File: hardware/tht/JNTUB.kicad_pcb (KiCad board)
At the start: 2 copper layers, 41.1 x 110.7 mm, 84 parts, among them J1 PARAM1_CV, J10 B2_HDR_LEFT, J11 B2_HDR_RIGHT, J12 ISP, J2 PARAM2_CV, J3 CLK/TRG, J4 DITTO, J5 OUT1, J6 OUT2, J7 B1_HDR_LEFT, J8 B1_HDR_RIGHT, J9 POWER, Q1 2N3904, Q2 2N3904, Q3 2N3904, U1 ATtiny85, U2 TL074, U3 78L05, U4 79L05

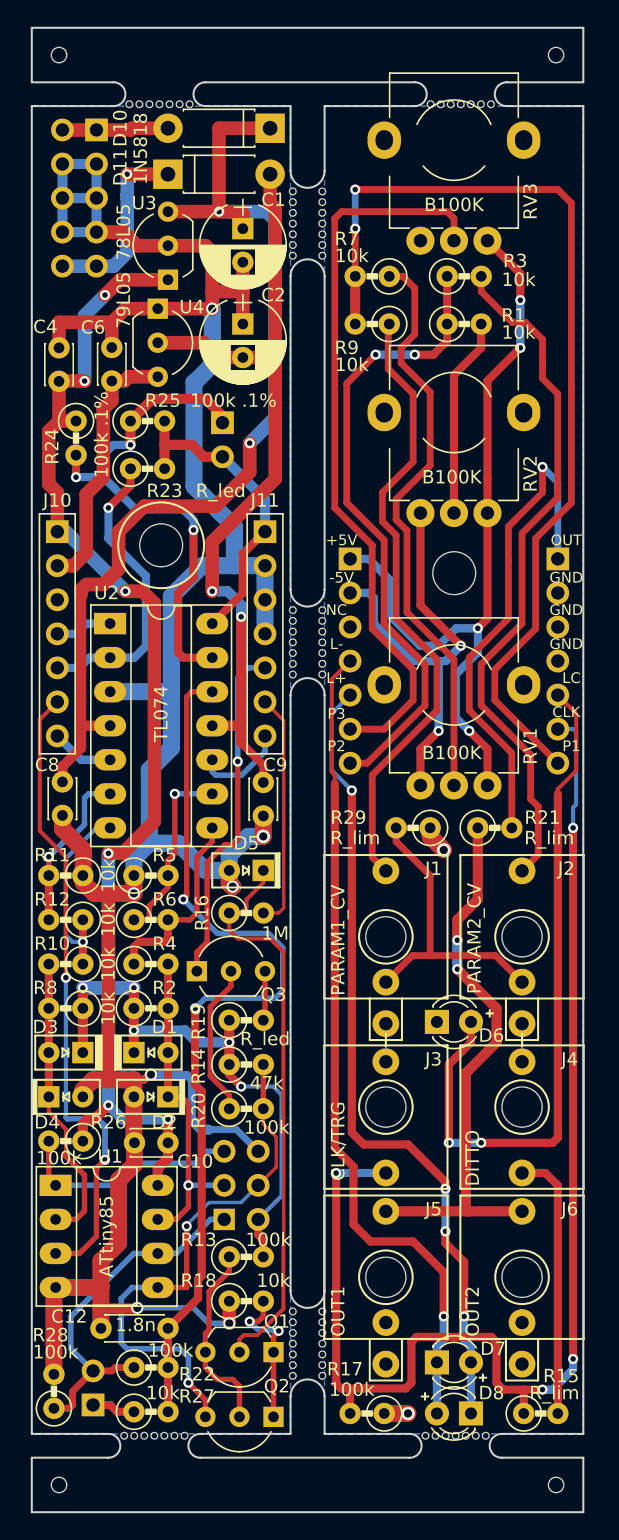
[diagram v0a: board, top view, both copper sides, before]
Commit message: Convert tht to KiCad 7. Update custom KiCad library paths.
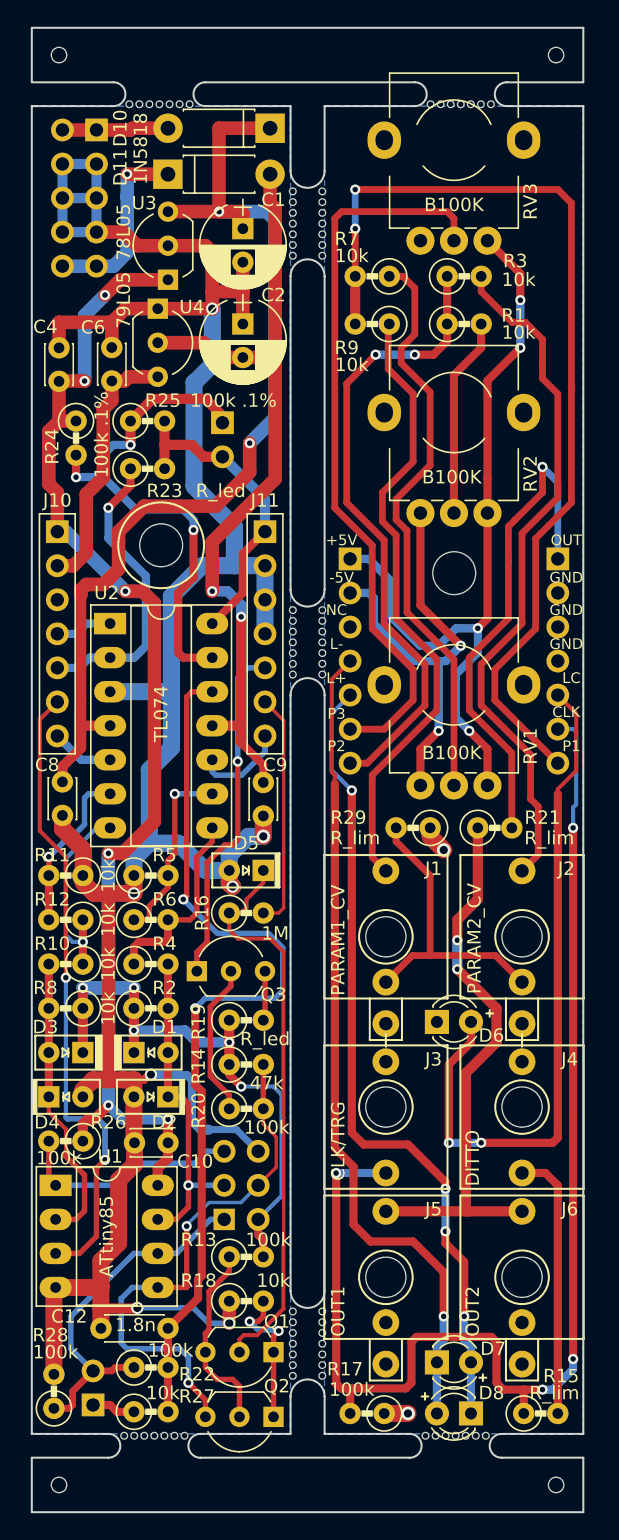
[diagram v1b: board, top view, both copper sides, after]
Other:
- net class Default removed
- net class Ground removed
- net class Medium removed
- net class Power removed
- net class Small removed
- net class Small and Close removed
